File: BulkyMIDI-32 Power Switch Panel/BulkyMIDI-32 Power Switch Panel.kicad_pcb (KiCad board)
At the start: 2 copper layers, 100 x 23.2 mm, 18 parts, among them J1 Switch Panel, M1 Mounting_Pin, M2 Mounting_Pin, M3 Mounting_Pin, M4 Mounting_Pin, SW1 CH1, SW2 CH2, SW3 CH3, SW4 CH4, SW5 CH5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

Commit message: Fixes panel errors and inconsistencies
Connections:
- SW1 pad 1: VCC -> GND
- SW2 pad 1: VCC -> GND
- SW3 pad 1: VCC -> GND
- SW4 pad 1: VCC -> GND
- SW5 pad 1: VCC -> GND
- SW6 pad 1: VCC -> GND
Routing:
- net VCC: track 247.3 -> 153.1 mm
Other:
- board text added: "BulkyMIDI-32 Power Switch Panel (rev. B) github.com/tebl"
- board text removed: "BulkyMIDI-32 Power Switch Panel (rev. A) github.com/tebl"

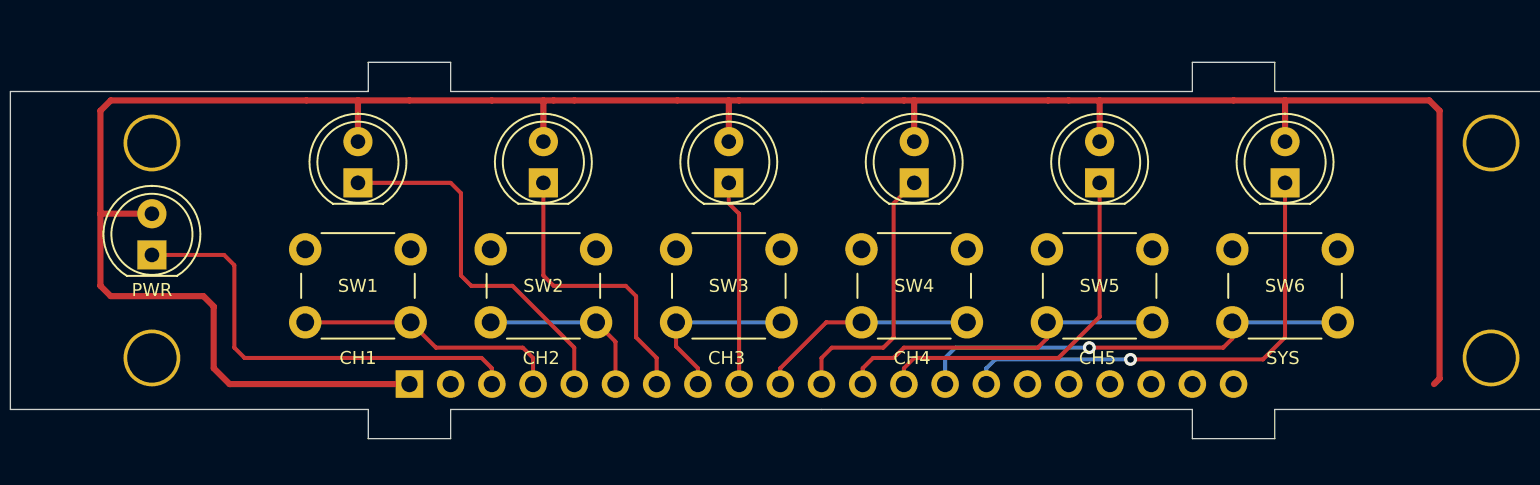
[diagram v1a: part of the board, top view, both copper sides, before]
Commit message: Updated Power Switch to incorporate changes
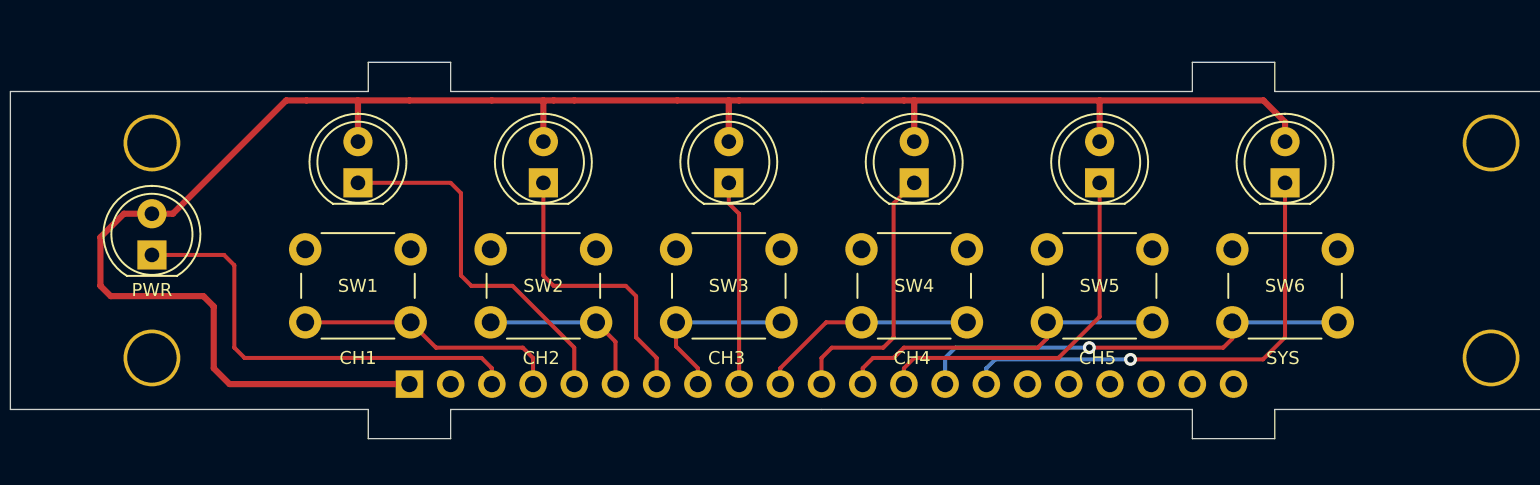
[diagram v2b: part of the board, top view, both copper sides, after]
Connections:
- J1 pad 16: (no net) -> unconnected-(J1-N.C.-Pad16)
- J1 pad 17: (no net) -> unconnected-(J1-N.C.-Pad17)
- J1 pad 18: (no net) -> unconnected-(J1-N.C.-Pad18)
- J1 pad 19: (no net) -> unconnected-(J1-N.C.-Pad19)
- J1 pad 21: (no net) -> unconnected-(J1-N.C.-Pad21)
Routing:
- net VCC: track 153.1 -> 117.8 mm
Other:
- net class Default removed
- net class PWR removed
